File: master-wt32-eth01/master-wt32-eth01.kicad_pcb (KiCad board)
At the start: 2 copper layers, 61 x 72.4 mm, 12 parts, among them J1 24V Field, J2 24V System, J3 Enable, J4 Screw_Terminal_01x03, J5 Conn_01x06_Female, J6 Conn_01x06_Female, SW1 SW_DIP_x03, U1 LM2596-Board, U2 WT32-ETH0-Board, U3 PC817

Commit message: add tracks to master-wt32-eth01
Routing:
- net +3V3: track 0.00 -> 108.2 mm
- net GPIO35: track 0.00 -> 95.2 mm
- net GND: track 0.00 -> 91.4 mm
- net GNDPWR: track 0.00 -> 82.0 mm
- net +24V: track 0.00 -> 75.5 mm
- net Net-(J2-Pad2): track 0.00 -> 73.2 mm
- net SCL: track 0.00 -> 62.4 mm
- net SDA: track 0.00 -> 51.7 mm
- net Net-(J2-Pad1): track 0.00 -> 48.9 mm
- net Net-(J3-Pad2): track 0.00 -> 41.3 mm
- net 1WIRE: track 0.00 -> 38.2 mm
- net GPIO36: track 0.00 -> 35.7 mm
- net GPIO15: track 0.00 -> 35.6 mm
- net GPIO14: track 0.00 -> 34.6 mm
- net GPIO4: track 0.00 -> 31.0 mm
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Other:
- net class Default: clearance 0.2 -> 0.25; trace_width 0.2 -> 0.25
- net class Power: clearance 0.2 -> 0.3
- rule trace_clearance: 0.2 -> 0.25

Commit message: v1.1
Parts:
- added C1: 1uF 50V, Capacitor_THT:CP_Radial_D5.0mm_P2.50mm, F.Cu at (103.6, 74.9)
- added C2: 1uF 50V, Capacitor_THT:CP_Radial_D5.0mm_P2.50mm, F.Cu at (103.6, 68.7)
- added C3: 100nF 63V, Capacitor_THT:C_Rect_L7.0mm_W2.0mm_P5.00mm, F.Cu at (69.2, 73.7)
- added C4: 100nF 63V, Capacitor_THT:C_Rect_L7.0mm_W2.0mm_P5.00mm, F.Cu at (98.6, 69.1)
- added D1: DB107, custom:DB107, F.Cu at (81.9, 68.2)
- added D2: DB107, custom:DB107, F.Cu at (91.3, 68.2)
- added H1: MountingHole, MountingHole:MountingHole_3.2mm_M3, F.Cu at (66.9, 58.0)
- added H2: MountingHole, MountingHole:MountingHole_3.2mm_M3, F.Cu at (129.9, 58.0)
- added H3: MountingHole, MountingHole:MountingHole_3.2mm_M3, F.Cu at (66.9, 123.6)
- added H4: MountingHole, MountingHole:MountingHole_3.2mm_M3, F.Cu at (106.3, 109.9)
- added R3: 100k, Resistor_THT:R_Axial_DIN0207_L6.3mm_D2.5mm_P7.62mm_Horizontal, F.Cu at (78.9, 100.8)
- U2: footprint boards:WT32-ETH0-Board -> boards:WT32-ETH01-Board-Reversed
- moved SW1 25.7 mm to (101.7, 90.6)
- moved R2 16.7 mm to (89.8, 100.8)
- moved U1 9.65 mm to (121.4, 83.8)
- moved J5 8.89 mm to (121.9, 99.1)
- moved J6 8.89 mm to (121.9, 121.9)
- moved J4 7.08 mm to (102.2, 119.8)
- moved U3 6.71 mm to (83.1, 100.8), turned to 90 degrees
- moved U2 5.46 mm to (83.9, 97.7)
- moved J1 5.39 mm to (79.4, 61.8)
- moved J2 5.39 mm to (89.5, 61.8)
- moved J3 5.39 mm to (99.7, 61.8)
- moved R1 4.89 mm to (87.9, 104.9), turned to 180 degrees
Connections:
- J1 pad 1: GNDPWR -> FIELD_IN-
- J1 pad 2: +24V -> FIELD_IN+
- J2 pad 1: Net-(J2-Pad1) -> SYSTEM_IN-
- J2 pad 2: Net-(J2-Pad2) -> SYSTEM_IN+
- SW1 pad 1: Net-(J2-Pad2) -> SYSTEM+
- SW1 pad 2: Net-(J2-Pad1) -> SYSTEM-
- U1 pad 1: Net-(J2-Pad2) -> SYSTEM+
- U1 pad 2: Net-(J2-Pad1) -> SYSTEM-
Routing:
- net SYSTEM+: track 0.00 -> 75.6 mm
- net Net-(J2-Pad2): track 73.2 -> 0.00 mm
- net GPIO35: track 95.2 -> 34.0 mm
- net SYSTEM-: track 0.00 -> 60.1 mm
- net Net-(J2-Pad1): track 48.9 -> 0.00 mm
- net SCL: track 62.4 -> 30.8 mm
- net GPIO4: track 31.0 -> 58.3 mm
- net GPIO5: track 31.0 -> 56.8 mm
- net GPIO36: track 35.7 -> 60.2 mm
- net GPIO14: track 34.6 -> 57.9 mm
- net GPIO15: track 35.6 -> 58.8 mm
- net +3V3: track 108.2 -> 86.4 mm
- net Net-(J3-Pad2): track 41.3 -> 59.8 mm
- net +24V: track 75.5 -> 90.3 mm
- net 1WIRE: track 38.2 -> 51.3 mm
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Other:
- board size 61 x 72.4 mm -> 69.9 x 72.4 mm
- board text added: "24V Field"
- board text added: "24V System"
- board text added: "Brick Master wt32-eth01 v1.1"
- board text removed: "Brick Master wt32-eth01"
- board text removed: "Field"
- board text removed: "System"

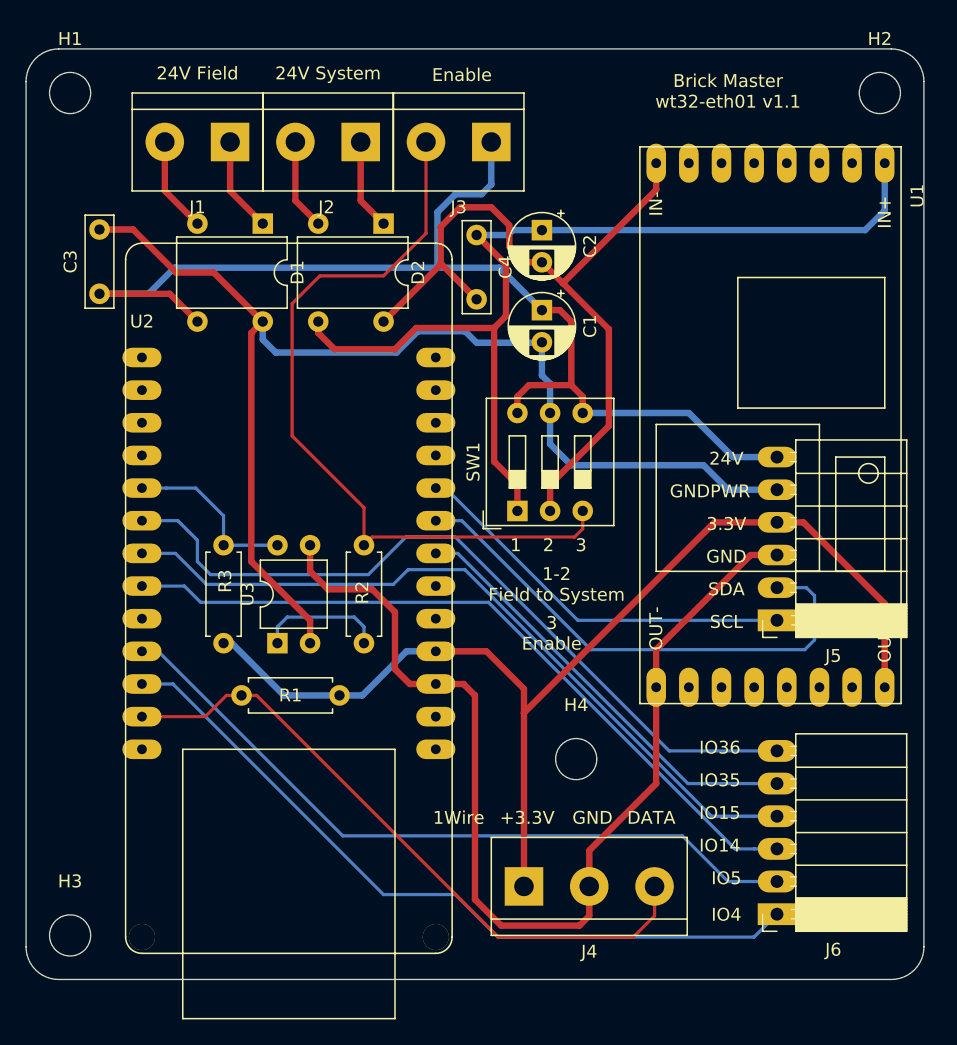
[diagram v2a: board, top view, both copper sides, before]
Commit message: move input/output connectors
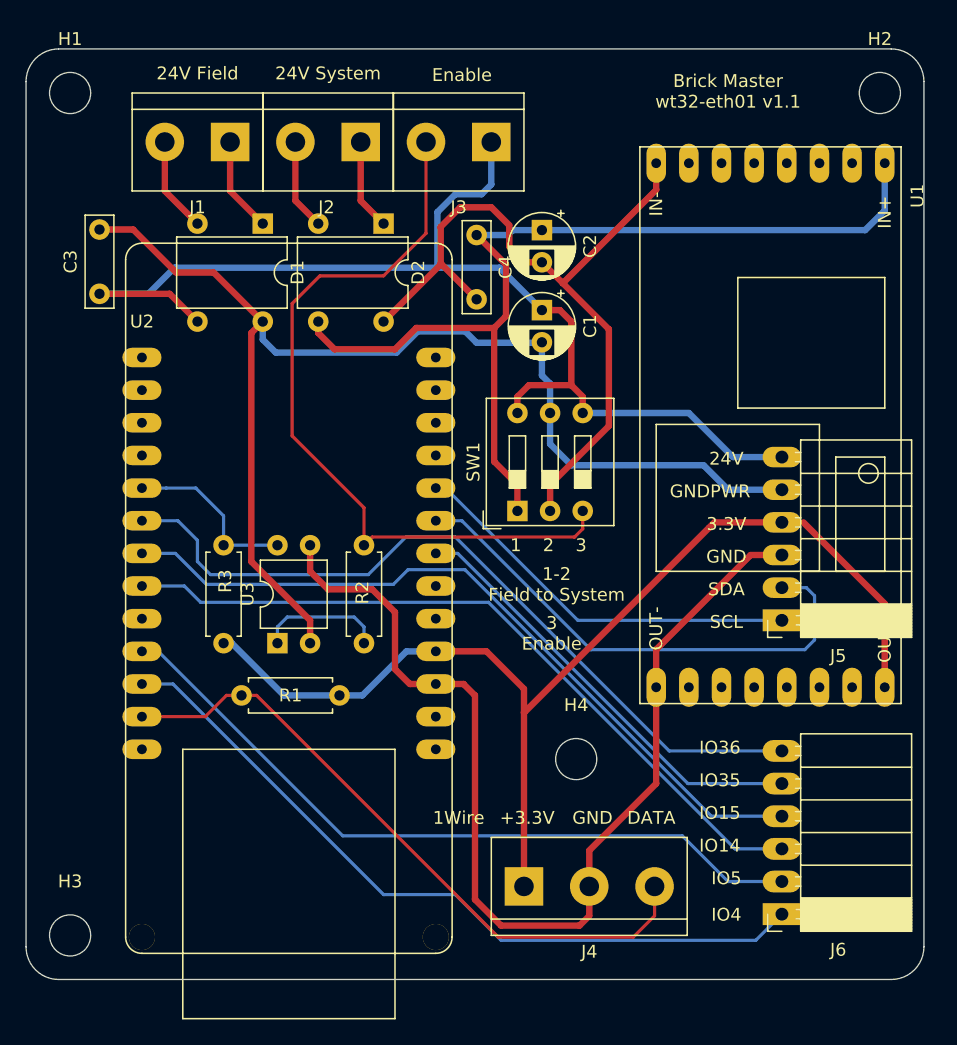
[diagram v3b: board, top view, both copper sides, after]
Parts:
- moved J5 0.38 mm to (122.3, 99.1)
- moved J6 0.38 mm to (122.3, 121.9)
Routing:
- net +3V3: track 86.4 -> 84.7 mm
- net GPIO4: track 58.3 -> 58.9 mm

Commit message: upgrade master-wt32-eth01 format
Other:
- net class Default removed
- net class Power removed

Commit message: refactor power
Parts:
- removed J2: 24V System, TerminalBlock:TerminalBlock_bornier-2_P5.08mm
- removed J3: Enable, TerminalBlock:TerminalBlock_bornier-2_P5.08mm
- C2: value 1uF 50V -> 100nF 50V; footprint Capacitor_THT:CP_Radial_D5.0mm_P2.50mm -> Capacitor_THT:C_Rect_L7.0mm_W2.0mm_P5.00mm
- C3: value 100nF 63V -> 1uF 50V; footprint Capacitor_THT:C_Rect_L7.0mm_W2.0mm_P5.00mm -> Capacitor_THT:CP_Radial_D5.0mm_P2.50mm
- J1: value 24V Field -> Screw_Terminal_01x06; footprint TerminalBlock:TerminalBlock_bornier-2_P5.08mm -> TerminalBlock:TerminalBlock_bornier-6_P5.08mm
- moved C3 38.1 mm to (107.3, 72.3)
- moved C4 17.2 mm to (114.9, 74.3), turned to 90 degrees
- moved C2 9.17 mm to (95.9, 73.6), turned to 90 degrees
- moved J1 4.56 mm to (74.9, 62.9), turned to 0 degrees
- moved C1 3.68 mm to (101.0, 72.4), turned to 90 degrees
- moved D1 0.41 mm to (81.8, 68.6)
- moved D2 0.38 mm to (91.3, 68.6)
- moved SW1 0.24 mm to (101.6, 90.8)
- moved U1 0.13 mm to (121.3, 83.8)
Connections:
- C2 pad 1: SYSTEM+ -> +24V
- C2 pad 2: SYSTEM- -> GNDPWR
- C3 pad 1: +24V -> +3V3
- C3 pad 2: GNDPWR -> GND
- C4 pad 1: SYSTEM+ -> +3V3
- C4 pad 2: SYSTEM- -> GND
- D1 pad 1: FIELD_IN- -> FIELD-
- D1 pad 2: FIELD_IN+ -> FIELD+
- D2 pad 1: SYSTEM_IN- -> SYSTEM-
- D2 pad 2: SYSTEM_IN+ -> SYSTEM+
- D2 pad 3: SYSTEM+ -> Net-(D2-Pad3)
- D2 pad 4: SYSTEM- -> Net-(D2-Pad4)
- J1 pad 1: FIELD_IN- -> FIELD+
- J1 pad 2: FIELD_IN+ -> FIELD-
- R2 pad 2: Net-(J3-Pad2) -> ENABLE_IN
- SW1 pad 1: SYSTEM+ -> FIELD+
- SW1 pad 2: SYSTEM- -> FIELD-
- SW1 pad 3: Net-(J3-Pad2) -> +24V
- SW1 pad 4: +24V -> ENABLE_IN
- SW1 pad 5: GNDPWR -> SYSTEM+
- SW1 pad 6: +24V -> SYSTEM+
- U1 pad 1: SYSTEM+ -> Net-(D2-Pad3)
- U1 pad 2: SYSTEM- -> Net-(D2-Pad4)
- U2 pad 1: Net-(U2-Pad1) -> unconnected-(U2-Pad1)
- U2 pad 12: Net-(U2-Pad12) -> unconnected-(U2-Pad12)
- U2 pad 13: Net-(U2-Pad13) -> unconnected-(U2-Pad13)
- U2 pad 14: Net-(U2-Pad14) -> unconnected-(U2-Pad14)
- U2 pad 18: Net-(U2-Pad18) -> unconnected-(U2-Pad18)
- U2 pad 2: Net-(U2-Pad2) -> unconnected-(U2-Pad2)
- U2 pad 23: Net-(U2-Pad23) -> unconnected-(U2-Pad23)
- U2 pad 24: Net-(U2-Pad24) -> unconnected-(U2-Pad24)
- U2 pad 25: Net-(U2-Pad25) -> unconnected-(U2-Pad25)
- U2 pad 26: Net-(U2-Pad26) -> unconnected-(U2-Pad26)
- U2 pad 3: Net-(U2-Pad3) -> unconnected-(U2-Pad3)
- U2 pad 4: Net-(U2-Pad4) -> unconnected-(U2-Pad4)
- U2 pad 8: Net-(U2-Pad8) -> unconnected-(U2-Pad8)
- U2 pad 9: Net-(U2-Pad9) -> unconnected-(U2-Pad9)
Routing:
- net GNDPWR: track 95.2 -> 0.00 mm
- net +24V: track 90.7 -> 0.00 mm
- net +3V3: track 84.7 -> 0.00 mm
- net GND: track 83.1 -> 0.00 mm
- net SYSTEM+: track 75.6 -> 0.00 mm
- net GPIO36: track 60.6 -> 0.00 mm
- net SYSTEM-: track 60.1 -> 0.00 mm
- net Net-(J3-Pad2): track 59.8 -> 0.00 mm
- net GPIO15: track 59.2 -> 0.00 mm
- net GPIO4: track 58.9 -> 0.00 mm
- net GPIO14: track 58.3 -> 0.00 mm
- net GPIO5: track 57.2 -> 0.00 mm
- net 1WIRE: track 51.3 -> 0.00 mm
- net SDA: track 40.2 -> 0.00 mm
- net GPIO35: track 34.3 -> 0.00 mm
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
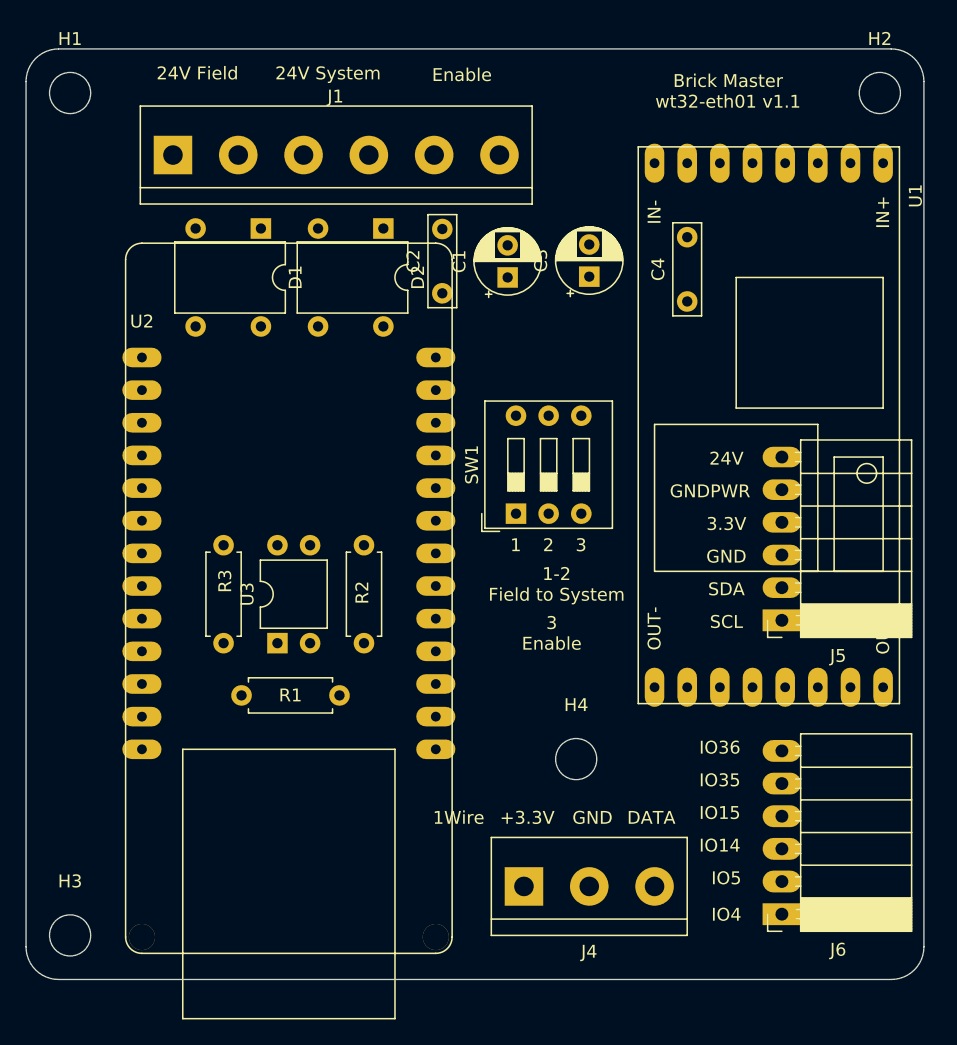
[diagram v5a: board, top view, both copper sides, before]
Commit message: add routing dragt to master-wt32-eth01
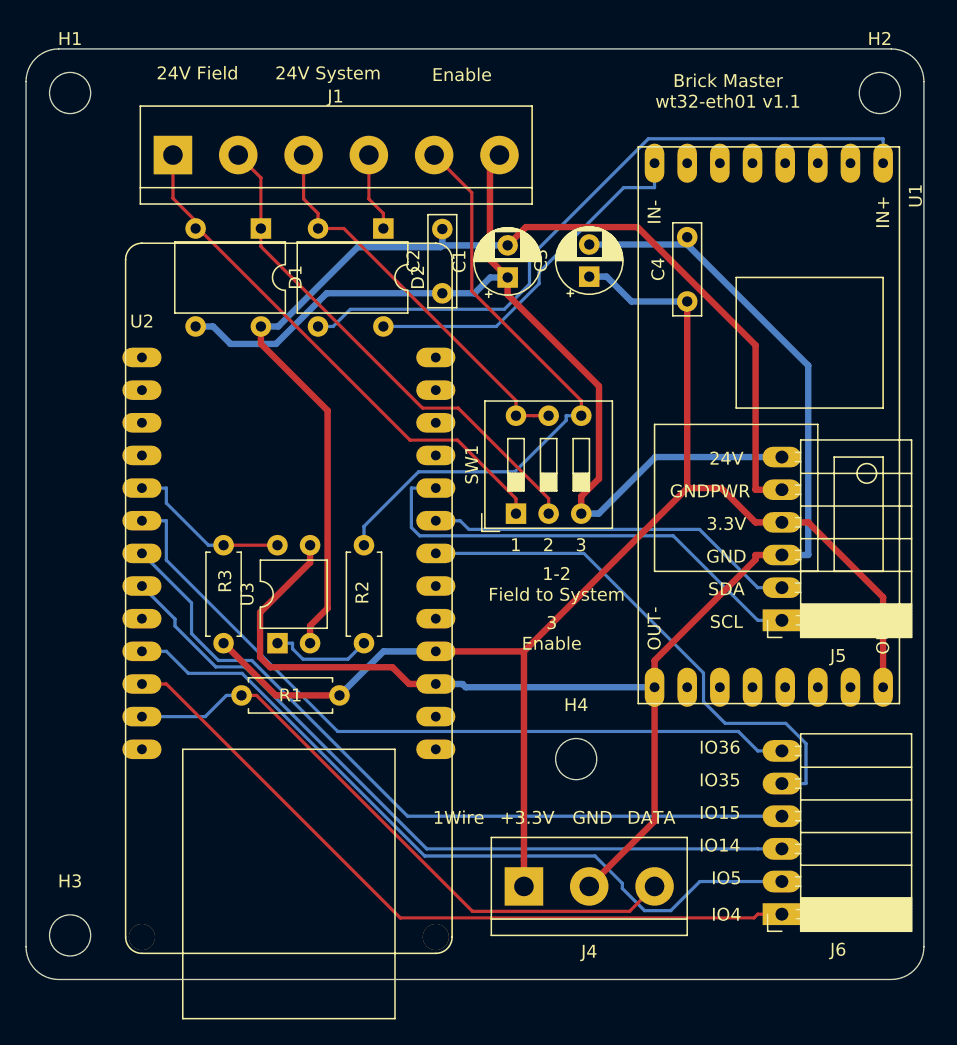
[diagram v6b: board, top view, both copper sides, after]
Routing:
- net GND: track 0.00 -> 113.5 mm
- net +3V3: track 0.00 -> 111.4 mm
- net GNDPWR: track 0.00 -> 87.4 mm
- net +24V: track 0.00 -> 76.7 mm
- net GPIO15: track 0.00 -> 59.6 mm
- net GPIO5: track 0.00 -> 59.3 mm
- net GPIO36: track 0.00 -> 59.0 mm
- net GPIO14: track 0.00 -> 58.6 mm
- net GPIO4: track 0.00 -> 57.4 mm
- net Net-(D2-Pad3): track 0.00 -> 53.1 mm
- net 1WIRE: track 0.00 -> 48.3 mm
- net ENABLE_IN: track 0.00 -> 47.2 mm
- net FIELD+: track 0.00 -> 41.7 mm
- net GPIO35: track 0.00 -> 41.2 mm
- net FIELD-: track 0.00 -> 39.5 mm
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
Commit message: fix power wiring in master-wt32-eth01
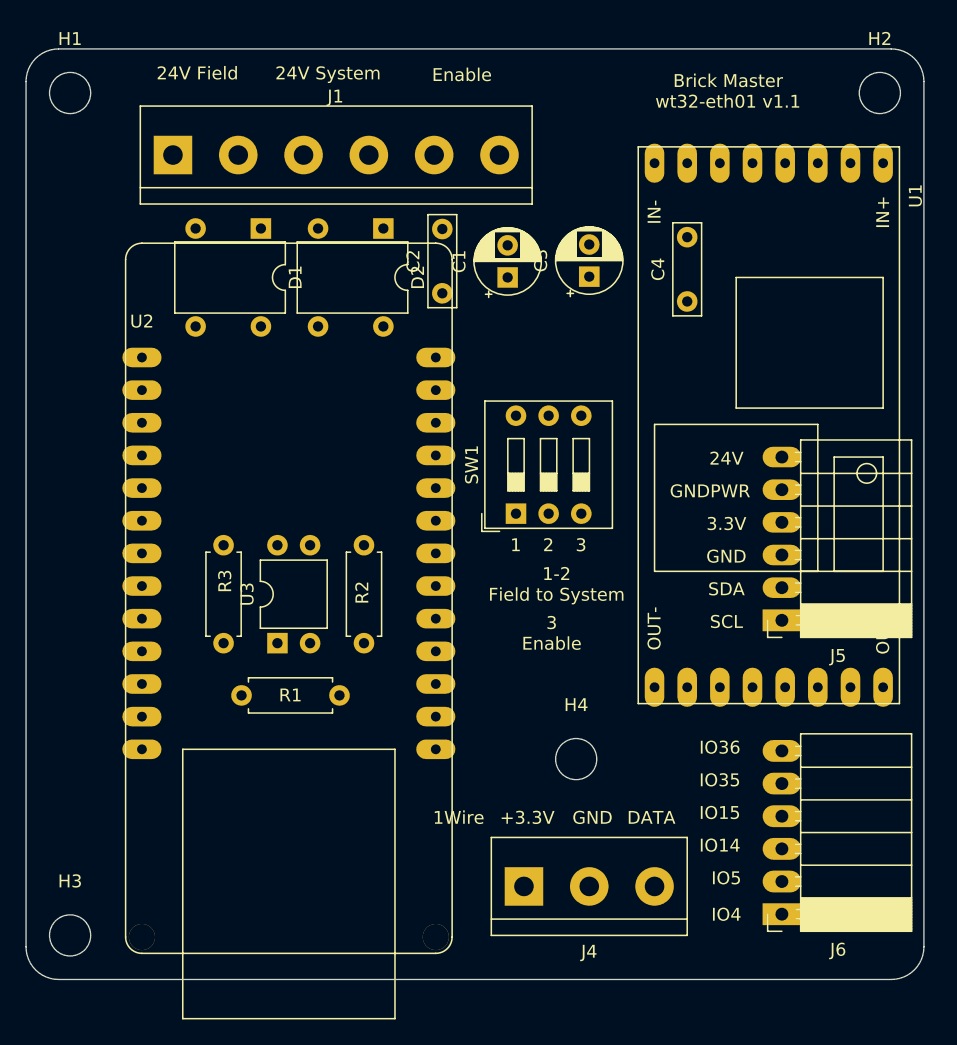
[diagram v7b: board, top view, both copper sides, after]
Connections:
- SW1 pad 5: SYSTEM+ -> SYSTEM-
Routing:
- net GND: track 113.5 -> 0.00 mm
- net +3V3: track 111.4 -> 0.00 mm
- net GNDPWR: track 87.4 -> 0.00 mm
- net +24V: track 76.7 -> 0.00 mm
- net GPIO15: track 59.6 -> 0.00 mm
- net GPIO5: track 59.3 -> 0.00 mm
- net GPIO36: track 59.0 -> 0.00 mm
- net GPIO14: track 58.6 -> 0.00 mm
- net GPIO4: track 57.4 -> 0.00 mm
- net Net-(D2-Pad3): track 53.1 -> 0.00 mm
- net 1WIRE: track 48.3 -> 0.00 mm
- net ENABLE_IN: track 47.2 -> 0.00 mm
- net FIELD+: track 41.7 -> 0.00 mm
- net GPIO35: track 41.2 -> 0.00 mm
- net FIELD-: track 39.5 -> 0.00 mm
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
